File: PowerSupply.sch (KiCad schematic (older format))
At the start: 15 parts, among them J1 Barrel_Jack_Switch, J2 Conn_02x02_Odd_Even, J3 Conn_02x02_Odd_Even, SW1 SW_DPDT_x2, U1 LM7805_TO220

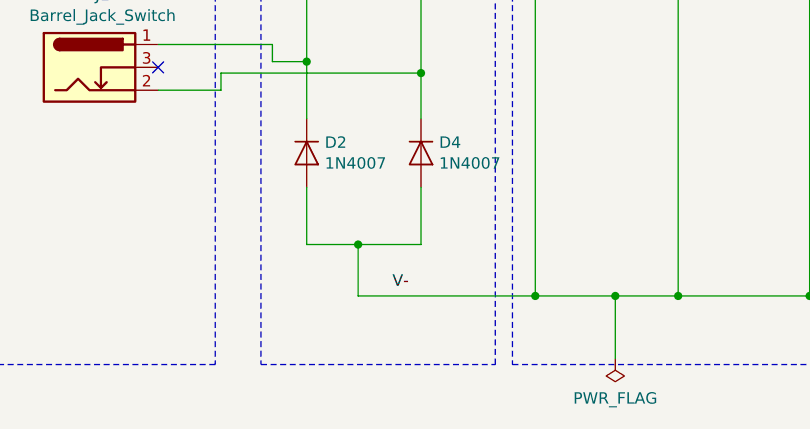
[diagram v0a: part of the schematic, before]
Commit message: Setup netlist and design rules for pcb
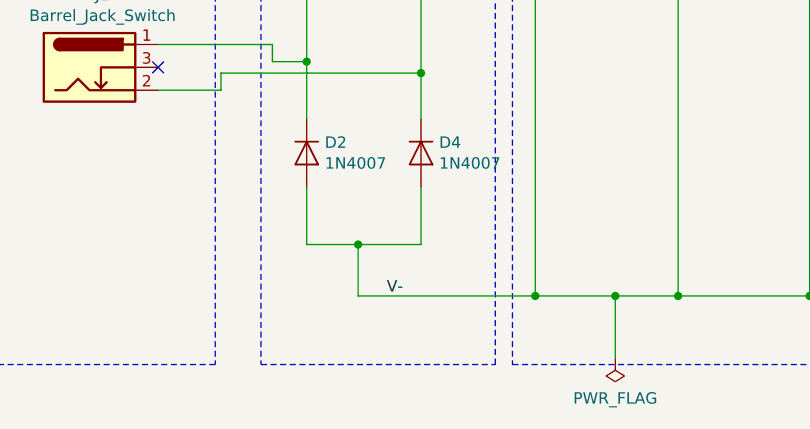
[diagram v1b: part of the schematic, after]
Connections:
- net V-: now also C1.2, C2.2, D2.2 (A), D4.2 (A), D5.1 (K), D6.1 (K), J2.3 (Pin_3), J2.4 (Pin_4), J3.3 (Pin_3), J3.4 (Pin_4), U1.2 (GND)
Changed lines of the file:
@@
 Text Label 4725 3350 0    50   ~ 0
 Vin
-Text Label 4800 5425 0    50   ~ 0
+Text Label 4775 5450 0    50   ~ 0
 V-
 Text Label 6750 3350 0    50   ~ 0
